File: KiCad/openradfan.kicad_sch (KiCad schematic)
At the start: 48 parts, among them CN1 DB141V-2.54-3P, CN2 DB141V-2.54-3P, J1 Fan_CPU_4pin, J2 Fan_CPU_4pin, J3 Fan_CPU_4pin, J4 Fan_CPU_4pin, J5 Fan_CPU_4pin, J6 Fan_CPU_4pin, J7 Fan_CPU_4pin, J8 Fan_CPU_4pin, Q1 AO3401A_C347476, U1 74AHCT125, U2 AP63205WU, U3 BTS462TATMA1, U4 Atom Lite

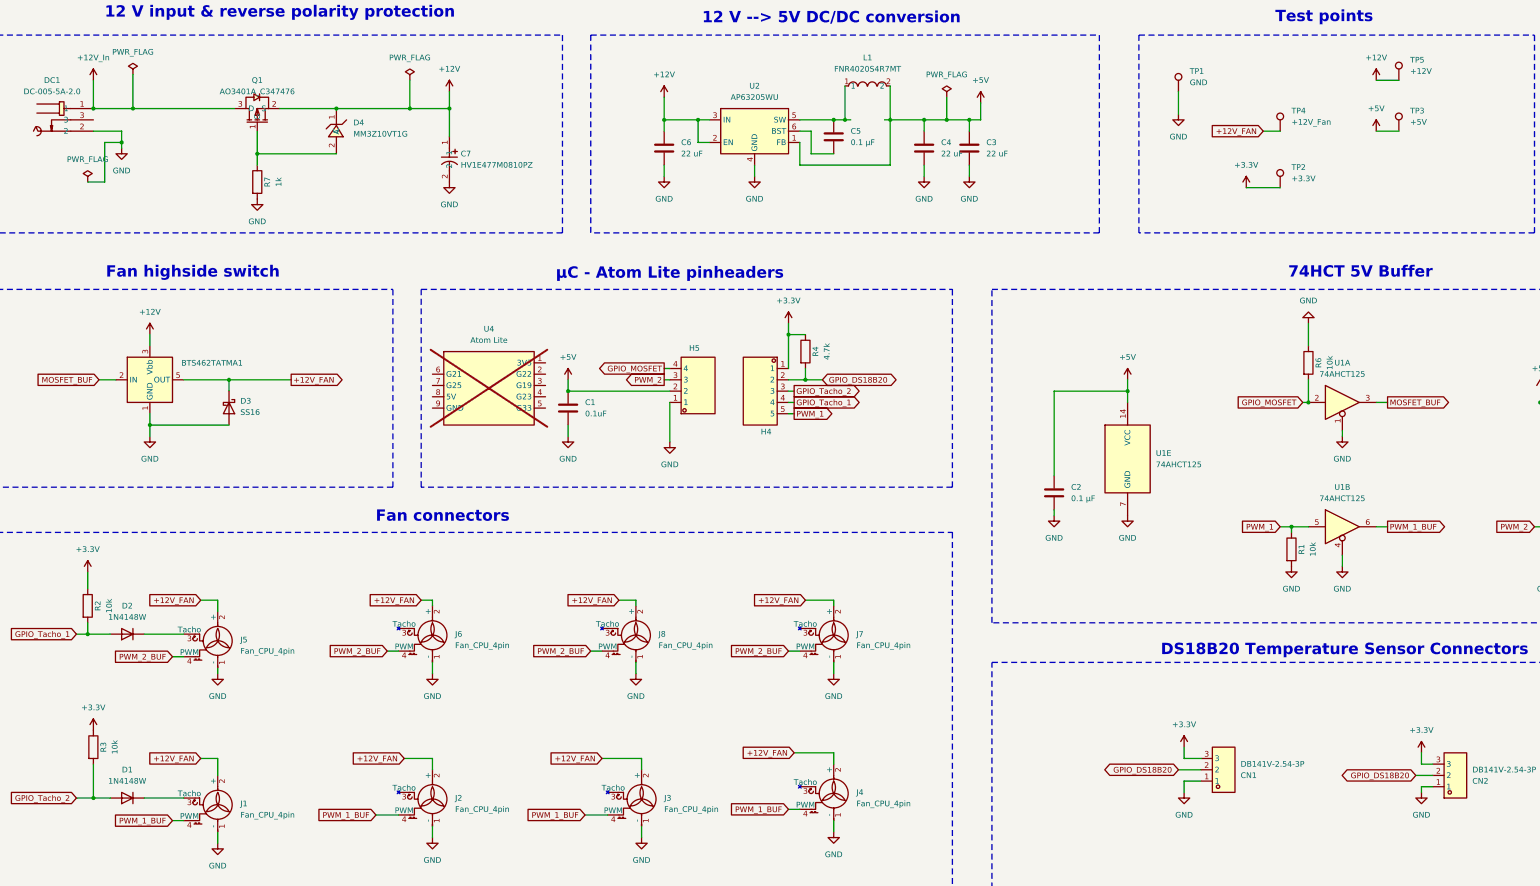
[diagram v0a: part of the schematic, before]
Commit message: Included safety components
Include reverse voltage protection, transient overvoltage protection & a resettable fuse
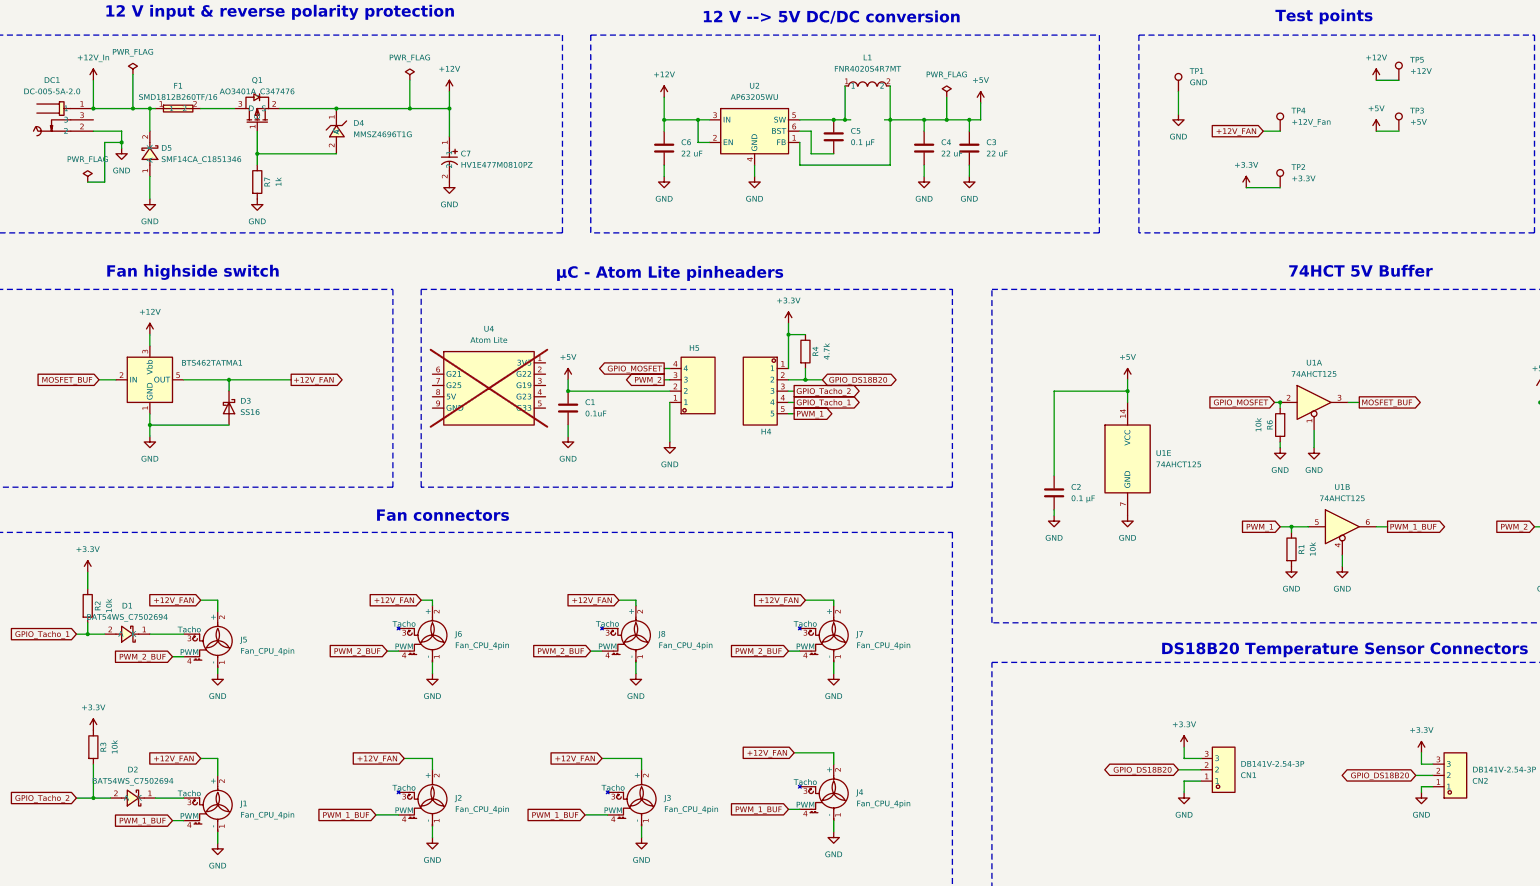
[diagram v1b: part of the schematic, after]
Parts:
- removed D1, D2: 1N4148W, Diode_SMD:D_SOD-123, symbol Diode:1N4148W
- removed D4: MM3Z10VT1G, easyeda2kicad:SOD-323_L1.8-W1.3-LS2.5-RD, symbol easyeda2kicad:MM3Z10VT1G
- added D1, D2: BAT54WS_C7502694, easyeda2kicad:SOD-323_L1.7-W1.3-LS2.6-RD-1, symbol easyeda2kicad:BAT54WS_C7502694
- added D4: MMSZ4696T1G, easyeda2kicad:SOD-123_L2.7-W1.6-LS3.7-RD-1, symbol easyeda2kicad:MMSZ4696T1G
- added D5: SMF14CA_C1851346, easyeda2kicad:SOD-123_L2.8-W1.8-LS3.7-BI, symbol easyeda2kicad:SMF14CA_C1851346
- added F1: SMD1812B260TF/16, easyeda2kicad:F1812, symbol easyeda2kicad:SMD1812B260TF_16
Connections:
- net +12V: now also D4.1 (C)
- net +12V_In: now also D5.2 (K), F1.1; no longer Q1.3 (D)
- net GND: now also D5.1 (A)
- net GPIO_Tacho_1: now also D1.2 (A)
- net GPIO_Tacho_2: now also D2.2 (A)
- net at Q1.1 (G), R7.1: now also D4.2 (A)
- net at J5.3 (Tacho): now also D1.1 (K)
- net at J1.3 (Tacho): now also D2.1 (K)
- new net: F1.2, Q1.3 (D)
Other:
- moved on the sheet: R6, U1A
